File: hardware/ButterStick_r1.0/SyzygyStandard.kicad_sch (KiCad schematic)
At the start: 19 parts, among them J4 SYZYGY-STD, U14 TLV62569DRL

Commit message: hw.r1d0: Review complete, gerbers generated
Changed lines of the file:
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@@
 (kicad_sch (version 20200618) (host eeschema "5.99.0-unknown-73168a9~101~ubuntu18.04.1")
-  (page 17 18)
+  (page 16 18)
   (paper "A4")
   (title_block
     (title "ButterStick")
-    (date "2020-07-16")
+    (date "2020-07-17")
     (rev "r1.0")
     (company "GsD")
@@
     (stroke (width 0) (type solid) (color 0 0 0 0))
   )
-  (bus (pts (xy 165.1 101.6) (xy 165.1 104.14))
-    (stroke (width 0) (type solid) (color 0 0 0 0))
-  )
-  (bus (pts (xy 165.1 104.14) (xy 165.1 109.22))
-    (stroke (width 0) (type solid) (color 0 0 0 0))
-  )
-  (bus (pts (xy 165.1 109.22) (xy 165.1 111.76))
+  (bus (pts (xy 165.1 101.6) (xy 165.1 106.68))
+    (stroke (width 0) (type solid) (color 0 0 0 0))
+  )
+  (bus (pts (xy 165.1 106.68) (xy 165.1 111.76))
     (stroke (width 0) (type solid) (color 0 0 0 0))
   )
@@
     (stroke (width 0) (type solid) (color 0 0 0 0))
   )
-  (bus (pts (xy 165.1 116.84) (xy 165.1 121.92))
-    (stroke (width 0) (type solid) (color 0 0 0 0))
-  )
-  (bus (pts (xy 165.1 121.92) (xy 165.1 127))
-    (stroke (width 0) (type solid) (color 0 0 0 0))
-  )
-  (bus (pts (xy 165.1 127) (xy 165.1 129.54))
-    (stroke (width 0) (type solid) (color 0 0 0 0))
-  )
-  (bus (pts (xy 165.1 129.54) (xy 165.1 134.62))
-    (stroke (width 0) (type solid) (color 0 0 0 0))
-  )
-  (bus (pts (xy 165.1 134.62) (xy 165.1 139.7))
-    (stroke (width 0) (type solid) (color 0 0 0 0))
-  )
-  (bus (pts (xy 165.1 139.7) (xy 165.1 153.67))
+  (bus (pts (xy 165.1 116.84) (xy 165.1 119.38))
+    (stroke (width 0) (type solid) (color 0 0 0 0))
+  )
+  (bus (pts (xy 165.1 119.38) (xy 165.1 124.46))
+    (stroke (width 0) (type solid) (color 0 0 0 0))
+  )
+  (bus (pts (xy 165.1 124.46) (xy 165.1 129.54))
+    (stroke (width 0) (type solid) (color 0 0 0 0))
+  )
+  (bus (pts (xy 165.1 129.54) (xy 165.1 132.08))
+    (stroke (width 0) (type solid) (color 0 0 0 0))
+  )
+  (bus (pts (xy 165.1 132.08) (xy 165.1 137.16))
+    (stroke (width 0) (type solid) (color 0 0 0 0))
+  )
+  (bus (pts (xy 165.1 137.16) (xy 165.1 147.32))
+    (stroke (width 0) (type solid) (color 0 0 0 0))
+  )
+  (bus (pts (xy 165.1 147.32) (xy 165.1 153.67))
     (stroke (width 0) (type solid) (color 0 0 0 0))
   )
@@
     (stroke (width 0) (type solid) (color 0 0 0 0))
   )
-  (bus (pts (xy 228.6 127) (xy 228.6 132.08))
-    (stroke (width 0) (type solid) (color 0 0 0 0))
-  )
-  (bus (pts (xy 228.6 132.08) (xy 228.6 137.16))
-    (stroke (width 0) (type solid) (color 0 0 0 0))
-  )
+  (bus (pts (xy 228.6 127) (xy 228.6 129.54))
+    (stroke (width 0) (type solid) (color 0 0 0 0))
+  )
+  (bus (pts (xy 228.6 129.54) (xy 228.6 134.62))
+    (stroke (width 0) (type solid) (color 0 0 0 0))
+  )
+  (bus (pts (xy 228.6 134.62) (xy 228.6 137.16))
+    (stroke (width 0) (type solid) (color 0 0 0 0))
+  )

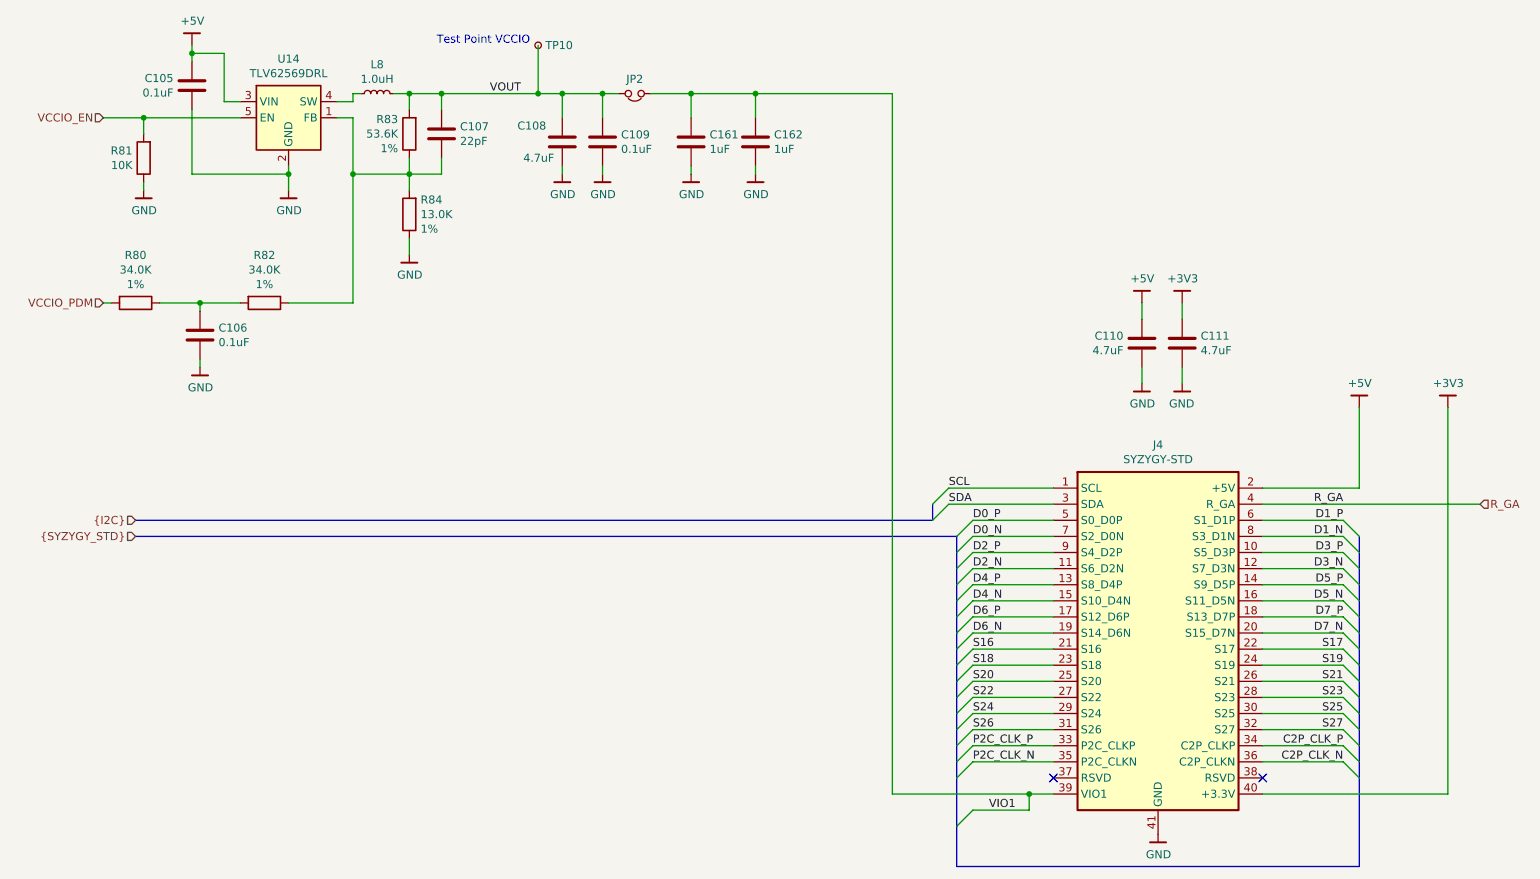
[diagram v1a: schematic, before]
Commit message: hw.r1d0: Update BOM fieids in schematic.
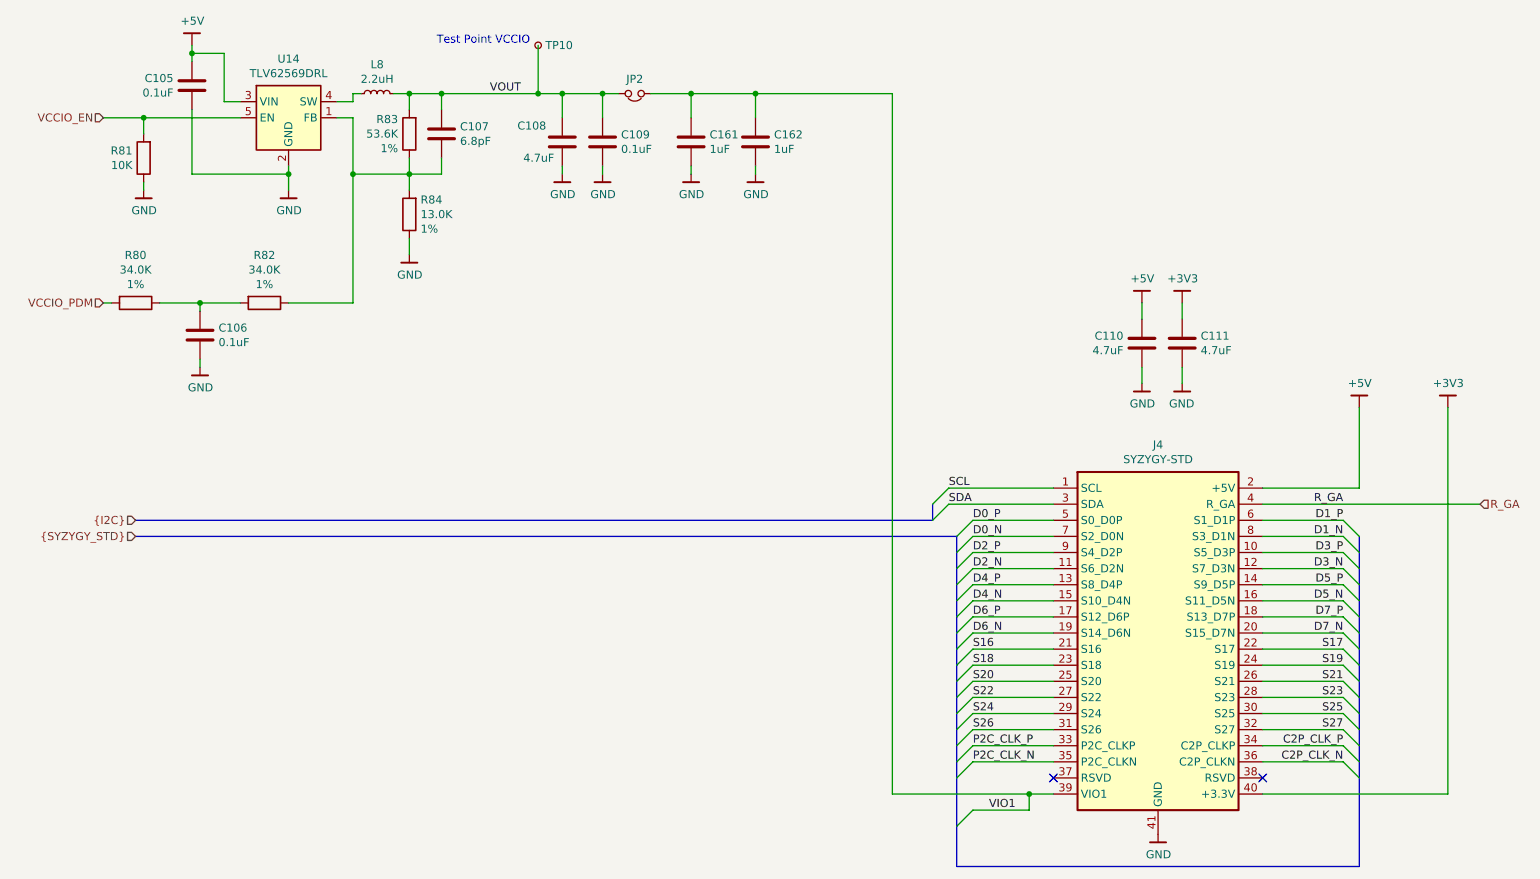
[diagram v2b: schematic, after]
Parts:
- C105, C109: Mfg Samsung Electro-Mechanics -> Yageo; PN CL05B104KP5NNNC -> CC0402KRX5R6BB104; Tol (none) -> 10V / X5R
- C106: Mfg Samsung Electro-Mechanics -> Yageo; PN (none) -> CC0402KRX5R6BB104; Tol (none) -> 10V / X5R
- C107: value 22pF -> 6.8pF; Mfg Samsung Electro-Mechanics -> Yageo; PN CL05B104KP5NNNC -> CC0402CRNPO9BN6R8
- C108, C110, C111: Mfg Samsung Electro-Mechanics -> Yageo; PN CL10A475KP8NNNC -> CC0603ZRY5V6BB475
- C161, C162: Mfg Samsung Electro-Mechanics -> Yageo; PN CL05B104KP5NNNC -> CC0402KRX5R6BB105
- L8: value 1.0uH -> 2.2uH; Mfg (none) -> Sunltech Tech; PN (none) -> SLM20122R2MIT
- R80, R82: Mfg Stackpole Electronics Inc -> Yageo; PN RNCF0402DTE10K0 -> RC0402FR-0734KL
- R81: Mfg Stackpole Electronics Inc -> Yageo; PN (none) -> RC0402FR-0710KL; Tol 1% -> (none)
- R83: Mfg Stackpole Electronics Inc -> Yageo; PN (none) -> RC0402FR-0753K6L
- R84: Mfg Stackpole Electronics Inc -> Yageo; PN (none) -> RC0402FR-0713KL
- TP10: PN (none) -> DNP
- U14: Mfg (none) -> Texas Instruments; PN (none) -> TLV62569DRLR

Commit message: hw.r1d0: Fix RGMII straps
This commit correctly sets the stop resistos on the RGMII lines to 1K5
instead of DNP.
Also regenerate and add a schematic in PDF format.

Fixes #6
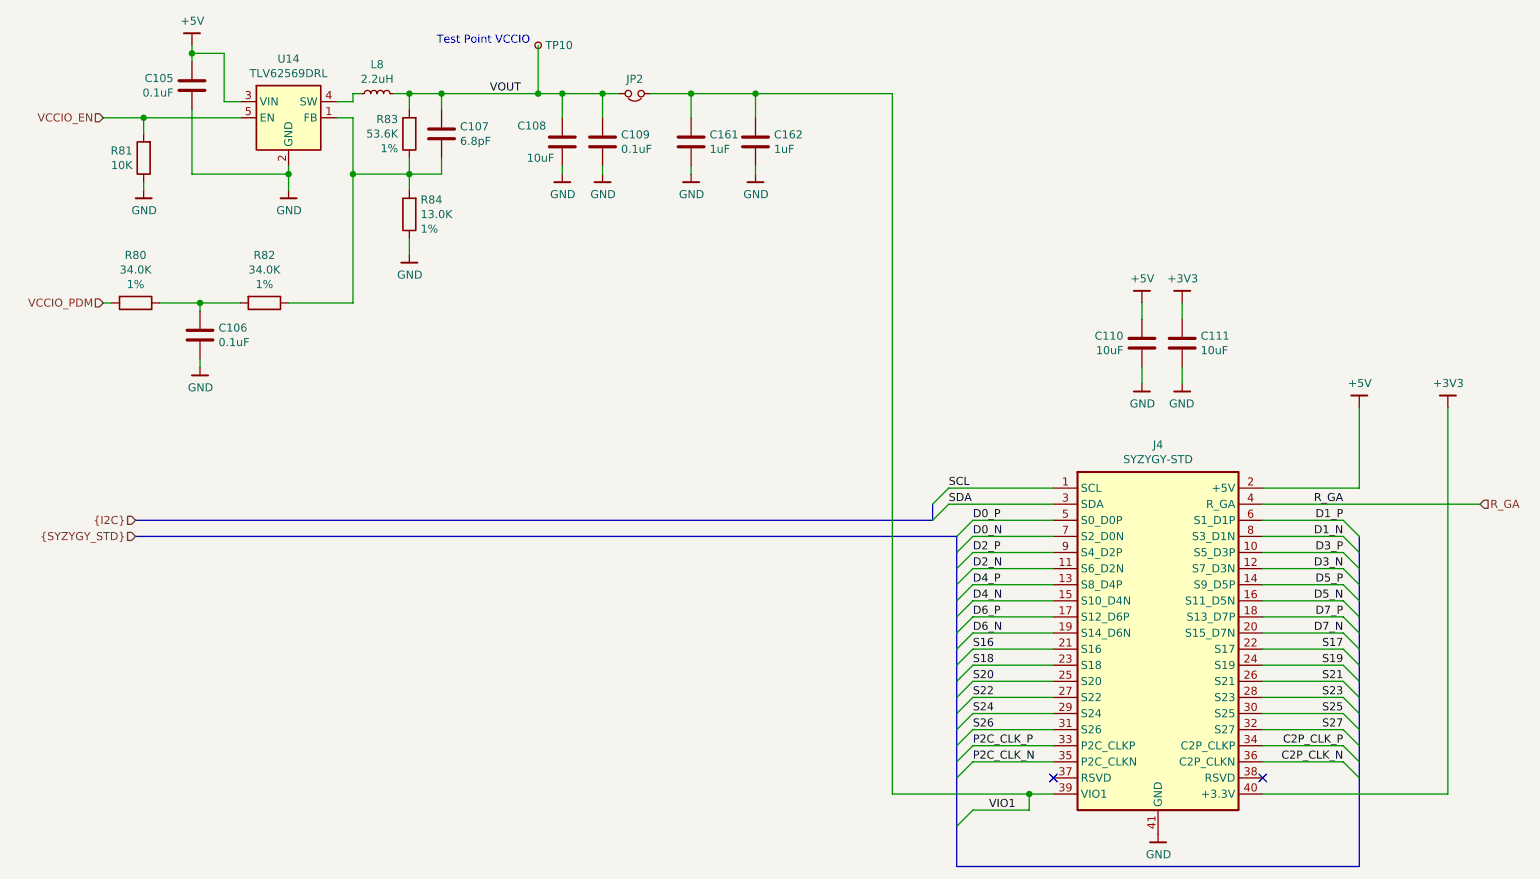
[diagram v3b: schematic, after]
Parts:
- C108, C110, C111: value 4.7uF -> 10uF; PN CC0603ZRY5V6BB475 -> CC0603KRX5R5BB106
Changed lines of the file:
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@@
-(kicad_sch (version 20200618) (host eeschema "5.99.0-unknown-73168a9~101~ubuntu18.04.1")
-  (page 1 18)
+(kicad_sch (version 20201015) (generator eeschema)
+  (page 0 18)
   (paper "A4")
   (title_block
     (title "ButterStick")
-    (date "2020-07-17")
+    (date "2020-11-01")
     (rev "r1.0")
     (company "GsD")
     (comment 1 "Functional prototyping board for the Lattice ECP5.")
-  )
-  (junction (at 36.83 35.56) (diameter 0) (color 0 0 0 0))
-  (junction (at 44.45 25.4) (diameter 0) (color 0 0 0 0))
-  (junction (at 45.72 64.77) (diameter 0) (color 0 0 0 0))
-  (junction (at 59.69 44.45) (diameter 0) (color 0 0 0 0))
-  (junction (at 69.85 44.45) (diameter 0) (color 0 0 0 0))
-  (junction (at 78.74 31.75) (diameter 0) (color 0 0 0 0))
-  (junction (at 78.74 44.45) (diameter 0) (color 0 0 0 0))
-  (junction (at 83.82 31.75) (diameter 0) (color 0 0 0 0))
-  (junction (at 99.06 31.75) (diameter 0) (color 0 0 0 0))
-  (junction (at 102.87 31.75) (diameter 0) (color 0 0 0 0))
-  (junction (at 109.22 31.75) (diameter 0) (color 0 0 0 0))
-  (junction (at 123.19 31.75) (diameter 0) (color 0 0 0 0))
-  (junction (at 133.35 31.75) (diameter 0) (color 0 0 0 0))
-  (junction (at 176.53 142.24) (diameter 0) (color 0 0 0 0))
+    (comment 2 "SYZYGY compatible")
+  )
+  (junction (at 36.83 35.56) (diameter 1.016) (color 0 0 0 0))
+  (junction (at 44.45 25.4) (diameter 1.016) (color 0 0 0 0))
+  (junction (at 45.72 64.77) (diameter 1.016) (color 0 0 0 0))
+  (junction (at 59.69 44.45) (diameter 1.016) (color 0 0 0 0))
+  (junction (at 69.85 44.45) (diameter 1.016) (color 0 0 0 0))
+  (junction (at 78.74 31.75) (diameter 1.016) (color 0 0 0 0))
+  (junction (at 78.74 44.45) (diameter 1.016) (color 0 0 0 0))
+  (junction (at 83.82 31.75) (diameter 1.016) (color 0 0 0 0))
+  (junction (at 99.06 31.75) (diameter 1.016) (color 0 0 0 0))
+  (junction (at 102.87 31.75) (diameter 1.016) (color 0 0 0 0))
+  (junction (at 109.22 31.75) (diameter 1.016) (color 0 0 0 0))
+  (junction (at 123.19 31.75) (diameter 1.016) (color 0 0 0 0))
+  (junction (at 133.35 31.75) (diameter 1.016) (color 0 0 0 0))
+  (junction (at 176.53 142.24) (diameter 1.016) (color 0 0 0 0))
   (no_connect (at 213.36 139.7))
   (no_connect (at 180.34 139.7))
@@
     (stroke (width 0) (type solid) (color 0 0 0 0))
   )
-  (bus (pts (xy 165.1 101.6) (xy 165.1 106.68))
+  (bus (pts (xy 165.1 101.6) (xy 165.1 104.14))
+    (stroke (width 0) (type solid) (color 0 0 0 0))
+  )
+  (bus (pts (xy 165.1 104.14) (xy 165.1 106.68))
     (stroke (width 0) (type solid) (color 0 0 0 0))
   )
@@
     (stroke (width 0) (type solid) (color 0 0 0 0))
   )
-  (bus (pts (xy 165.1 109.22) (xy 165.1 114.3))
-    (stroke (width 0) (type solid) (color 0 0 0 0))
-  )
-  (bus (pts (xy 165.1 114.3) (xy 165.1 119.38))
+  (bus (pts (xy 165.1 109.22) (xy 165.1 111.76))
+    (stroke (width 0) (type solid) (color 0 0 0 0))
+  )
+  (bus (pts (xy 165.1 111.76) (xy 165.1 114.3))
+    (stroke (width 0) (type solid) (color 0 0 0 0))
+  )
+  (bus (pts (xy 165.1 114.3) (xy 165.1 116.84))
+    (stroke (width 0) (type solid) (color 0 0 0 0))
+  )
+  (bus (pts (xy 165.1 116.84) (xy 165.1 119.38))
     (stroke (width 0) (type solid) (color 0 0 0 0))
   )
@@
     (stroke (width 0) (type solid) (color 0 0 0 0))
   )
-  (bus (pts (xy 165.1 121.92) (xy 165.1 127))
-    (stroke (width 0) (type solid) (color 0 0 0 0))
-  )
-  (bus (pts (xy 165.1 127) (xy 165.1 132.08))
-    (stroke (width 0) (type solid) (color 0 0 0 0))
-  )
-  (bus (pts (xy 165.1 132.08) (xy 165.1 137.16))
-    (stroke (width 0) (type solid) (color 0 0 0 0))
-  )
-  (bus (pts (xy 165.1 137.16) (xy 165.1 147.32))
+  (bus (pts (xy 165.1 121.92) (xy 165.1 124.46))
+    (stroke (width 0) (type solid) (color 0 0 0 0))
+  )
+  (bus (pts (xy 165.1 124.46) (xy 165.1 127))
+    (stroke (width 0) (type solid) (color 0 0 0 0))
+  )
+  (bus (pts (xy 165.1 127) (xy 165.1 129.54))
+    (stroke (width 0) (type solid) (color 0 0 0 0))
+  )
+  (bus (pts (xy 165.1 129.54) (xy 165.1 132.08))
+    (stroke (width 0) (type solid) (color 0 0 0 0))
+  )
+  (bus (pts (xy 165.1 132.08) (xy 165.1 134.62))
+    (stroke (width 0) (type solid) (color 0 0 0 0))
+  )
+  (bus (pts (xy 165.1 134.62) (xy 165.1 137.16))
+    (stroke (width 0) (type solid) (color 0 0 0 0))
+  )
+  (bus (pts (xy 165.1 137.16) (xy 165.1 139.7))
+    (stroke (width 0) (type solid) (color 0 0 0 0))
+  )
+  (bus (pts (xy 165.1 139.7) (xy 165.1 147.32))
     (stroke (width 0) (type solid) (color 0 0 0 0))
   )
@@
     (stroke (width 0) (type solid) (color 0 0 0 0))
   )
-  (bus (pts (xy 228.6 101.6) (xy 228.6 106.68))
-    (stroke (width 0) (type solid) (color 0 0 0 0))
-  )
-  (bus (pts (xy 228.6 106.68) (xy 228.6 111.76))
-    (stroke (width 0) (type solid) (color 0 0 0 0))
-  )
-  (bus (pts (xy 228.6 111.76) (xy 228.6 116.84))
-    (stroke (width 0) (type solid) (color 0 0 0 0))
-  )
-  (bus (pts (xy 228.6 116.84) (xy 228.6 121.92))
-    (stroke (width 0) (type solid) (color 0 0 0 0))
-  )
-  (bus (pts (xy 228.6 121.92) (xy 228.6 127))
+  (bus (pts (xy 228.6 101.6) (xy 228.6 104.14))
+    (stroke (width 0) (type solid) (color 0 0 0 0))
+  )
+  (bus (pts (xy 228.6 104.14) (xy 228.6 106.68))
+    (stroke (width 0) (type solid) (color 0 0 0 0))
+  )
+  (bus (pts (xy 228.6 106.68) (xy 228.6 109.22))
+    (stroke (width 0) (type solid) (color 0 0 0 0))
+  )
+  (bus (pts (xy 228.6 109.22) (xy 228.6 111.76))
+    (stroke (width 0) (type solid) (color 0 0 0 0))
+  )
+  (bus (pts (xy 228.6 111.76) (xy 228.6 114.3))
+    (stroke (width 0) (type solid) (color 0 0 0 0))
+  )
+  (bus (pts (xy 228.6 114.3) (xy 228.6 116.84))
+    (stroke (width 0) (type solid) (color 0 0 0 0))
+  )
+  (bus (pts (xy 228.6 116.84) (xy 228.6 119.38))
+    (stroke (width 0) (type solid) (color 0 0 0 0))
+  )
+  (bus (pts (xy 228.6 119.38) (xy 228.6 121.92))
+    (stroke (width 0) (type solid) (color 0 0 0 0))
+  )
+  (bus (pts (xy 228.6 121.92) (xy 228.6 124.46))
+    (stroke (width 0) (type solid) (color 0 0 0 0))
+  )
+  (bus (pts (xy 228.6 124.46) (xy 228.6 127))
     (stroke (width 0) (type solid) (color 0 0 0 0))
   )
@@
     (stroke (width 0) (type solid) (color 0 0 0 0))
   )
-  (bus (pts (xy 228.6 129.54) (xy 228.6 134.62))
+  (bus (pts (xy 228.6 129.54) (xy 228.6 132.08))
+    (stroke (width 0) (type solid) (color 0 0 0 0))
+  )
+  (bus (pts (xy 228.6 132.08) (xy 228.6 134.62))
     (stroke (width 0) (type solid) (color 0 0 0 0))
   )
@@
     (stroke (width 0) (type solid) (color 0 0 0 0))
   )
-  (bus (pts (xy 228.6 137.16) (xy 228.6 153.67))
+  (bus (pts (xy 228.6 137.16) (xy 228.6 139.7))
+    (stroke (width 0) (type solid) (color 0 0 0 0))
+  )
+  (bus (pts (xy 228.6 139.7) (xy 228.6 153.67))
     (stroke (width 0) (type solid) (color 0 0 0 0))
   )
@@
       (effects (font (size 1.27 1.27)) (justify right))
     )
-    (property "Value" "4.7uF" (id 1) (at 101.6 41.91 0)
+    (property "Value" "10uF" (id 1) (at 101.6 41.91 0)
       (effects (font (size 1.27 1.27)) (justify right))
     )
@@
       (effects (font (size 1.27 1.27)) hide)
     )
-    (property "PN" "CC0603ZRY5V6BB475" (id 5) (at -17.78 171.45 0)
+    (property "PN" "CC0603KRX5R5BB106" (id 5) (at -17.78 171.45 0)
       (effects (font (size 1.27 1.27)) hide)
     )
@@
       (effects (font (size 1.27 1.27)) (justify right))
     )
-    (property "Value" "4.7uF" (id 1) (at 191.389 72.263 0)
+    (property "Value" "10uF" (id 1) (at 191.389 72.263 0)
       (effects (font (size 1.27 1.27)) (justify right))
     )
@@
       (effects (font (size 1.27 1.27)) hide)
     )
-    (property "PN" "CC0603ZRY5V6BB475" (id 5) (at 73.66 203.2 0)
+    (property "PN" "CC0603KRX5R5BB106" (id 5) (at 73.66 203.2 0)
       (effects (font (size 1.27 1.27)) hide)
     )
@@
       (effects (font (size 1.27 1.27)) (justify right))
     )
-    (property "Value" "4.7uF" (id 1) (at 203.581 72.263 0)
+    (property "Value" "10uF" (id 1) (at 203.581 72.263 0)
       (effects (font (size 1.27 1.27)) (justify right))
     )
@@
       (effects (font (size 1.27 1.27)) hide)
     )
-    (property "PN" "CC0603ZRY5V6BB475" (id 5) (at 321.31 203.2 0)
-      (effects (font (size 1.27 1.27)) hide)
-    )
+    (property "PN" "CC0603KRX5R5BB106" (id 5) (at 321.31 203.2 0)
+      (effects (font (size 1.27 1.27)) hide)
+    )
